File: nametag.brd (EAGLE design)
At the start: 33 x 20.3 mm, 23 parts, among them U1 MCP73831

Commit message: updated routes
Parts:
- D2: value (none) -> 3V
- LIPO: value LiPo Battery -> (none)
- moved IC1 22.2 mm to (14.0, 10.2), turned to 180 degrees
- moved PRO_MICRO 22.2 mm to (16.5, 10.2)
- moved TILT_SWITCH 21.9 mm to (26.0, 10.5), flipped to the bottom, turned to 180 degrees
- moved R9 21.9 mm to (12.1, 14.9), turned to 0 degrees
- moved C4 7.67 mm to (25.4, 6.35), flipped to the bottom, turned to 180 degrees
- moved C1 7.04 mm to (27.3, 7.30)
- moved D2 4.55 mm to (30.8, 1.91)
- moved R10 4.09 mm to (24.8, 8.89)
- moved R7 2.29 mm to (12.7, 5.08)
- moved R4 2.25 mm to (17.5, 14.9), turned to 0 degrees
- moved LIPO 2.03 mm to (5.08, 3.10), turned to 90 degrees
- moved R5 1.80 mm to (15.2, 5.71)
- moved R8 1.80 mm to (10.2, 5.08)
- moved R2 1.80 mm to (22.9, 14.6), turned to 0 degrees
- moved C2 1.55 mm to (24.4, 5.40)
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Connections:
- removed net D2: U1.1
- new net STAT: PRO_MICRO.10, U1.1
- new net VCC: PRO_MICRO.21, R9.2
- net +3V3: now also POWER.2; no longer POWER.1, PRO_MICRO.21, R9.2
- net GND: now also LIPO.2; no longer LIPO.1
- net LIPO: now also LIPO.1, POWER.1; no longer LIPO.2, POWER.2
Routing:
- net +3V3: track 0.00 -> 68.1 mm, vias 0 -> 3
- net WRITE: track 0.00 -> 33.0 mm, vias 0 -> 2
- net DATA: track 0.00 -> 31.8 mm, vias 0 -> 2
- net TILT: track 0.00 -> 29.1 mm, vias 0 -> 2
- net READ: track 0.00 -> 27.1 mm, vias 0 -> 2
- net COL2: track 0.00 -> 24.5 mm, vias 0 -> 1
- net COL3: track 0.00 -> 24.1 mm, vias 0 -> 1
- net STAT: track 0.00 -> 22.3 mm, vias 0 -> 3
- net CS: track 0.00 -> 21.4 mm, vias 0 -> 2
- net COL0: track 0.00 -> 15.0 mm, vias 0 -> 1
- net VIN: track 0.00 -> 14.5 mm
- net COL1: track 0.00 -> 14.0 mm, vias 0 -> 1
- net ROW7: track 0.00 -> 13.3 mm, vias 0 -> 1
- net ROW5: track 0.00 -> 12.9 mm, vias 0 -> 1
- net ROW6: track 0.00 -> 12.7 mm, vias 0 -> 1
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
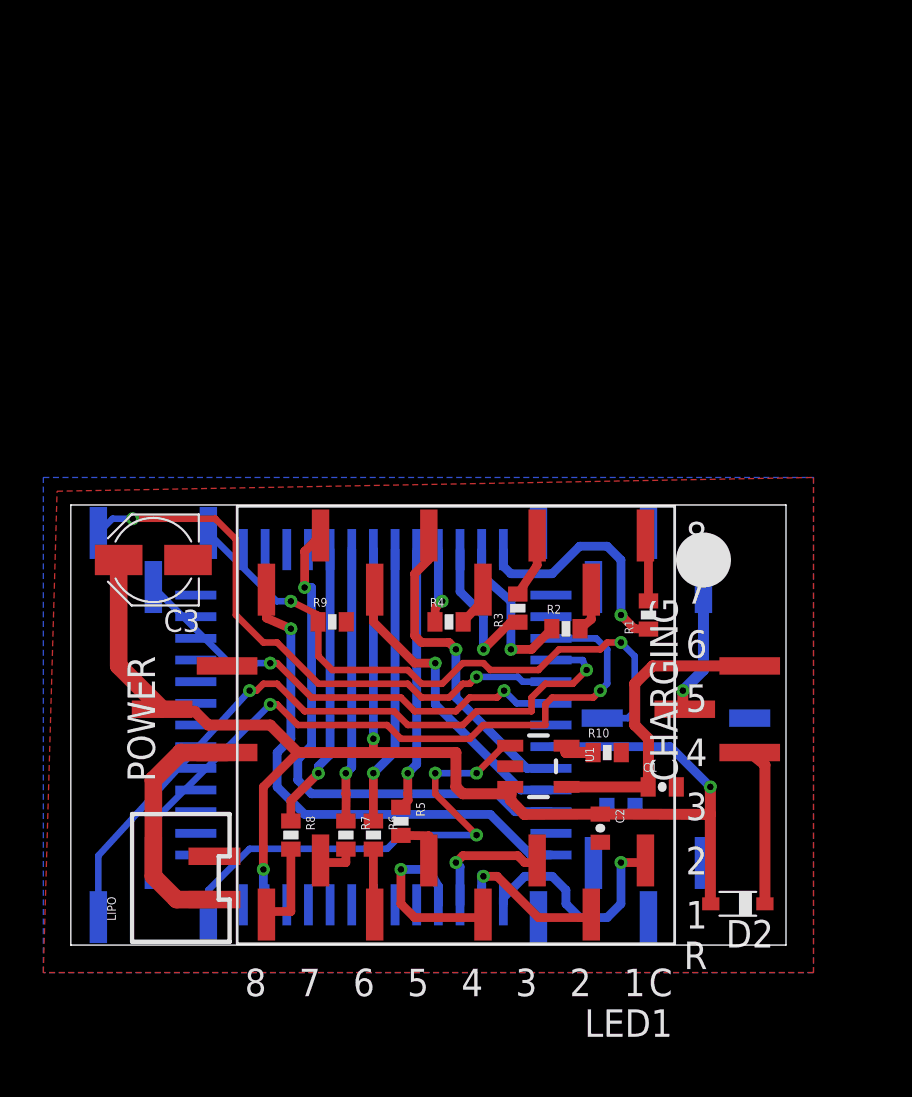
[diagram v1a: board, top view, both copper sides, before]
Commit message: added logos
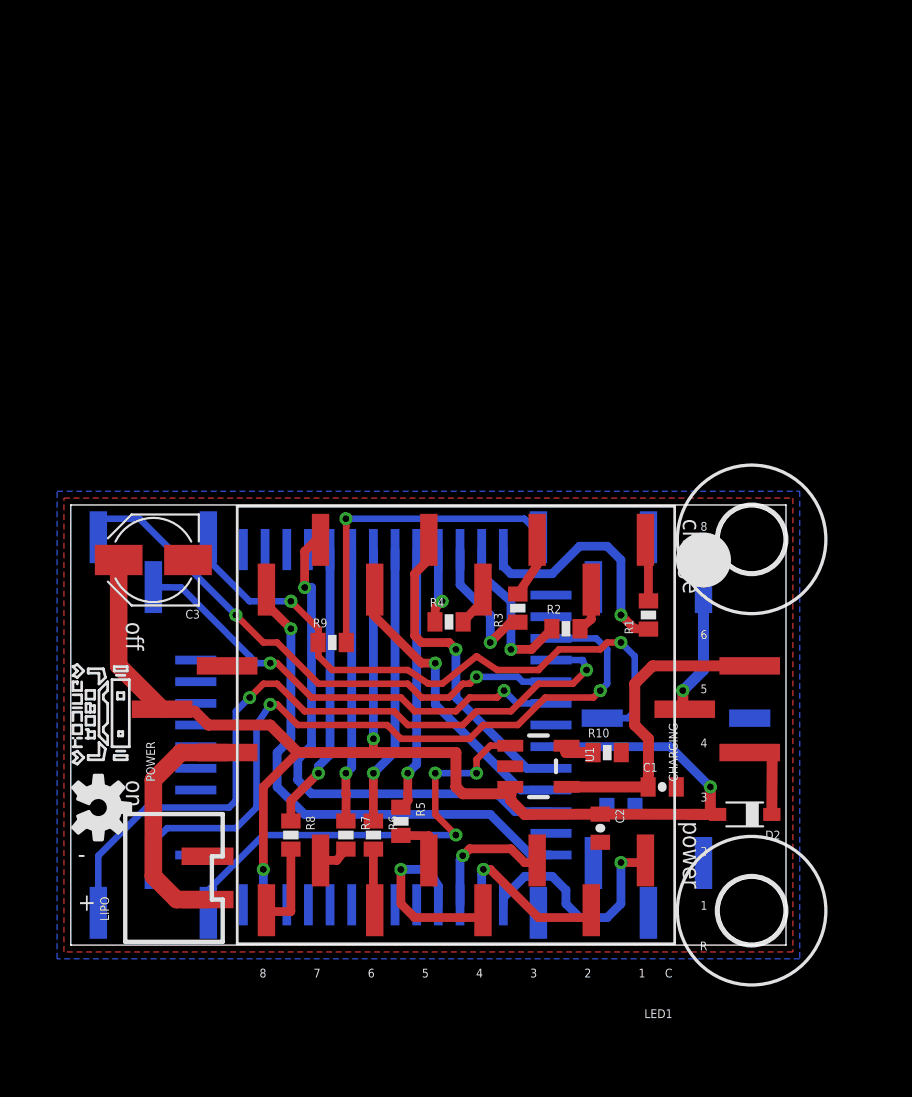
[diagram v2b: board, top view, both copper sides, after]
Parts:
- added E$1: (no value), Sumorobot:ROBOKODING-LOGO-S
- added LOGO1: OSHW-LOGOS, SparkFun-Aesthetics:OSHW-LOGO-S
- added U$1, U$2: (no value), holes:3,0
- moved D2 4.14 mm to (31.1, 6.03)
- moved R9 0.95 mm to (12.1, 14.0)
- moved LIPO 0.32 mm to (4.76, 3.10)
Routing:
- net VCC: track 0.00 -> 15.1 mm, vias 0 -> 1
- net +3V3: track 68.1 -> 64.6 mm
- net N$3: track 7.32 -> 3.98 mm
- net WRITE: track 33.0 -> 34.9 mm
- net READ: track 27.1 -> 25.6 mm
- net TILT: track 29.1 -> 30.5 mm
- net DATA: track 31.8 -> 33.0 mm
- net STAT: track 22.3 -> 21.3 mm
- net ROW2: track 7.17 -> 6.53 mm
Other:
- board text added: "+"
- board text added: "-"
- board text added: "NAMETAG v1.0"
- board text added: "charge"
- board text added: "off"
- board text added: "on"
- board text added: "power"

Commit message: updated nametag schematic and board
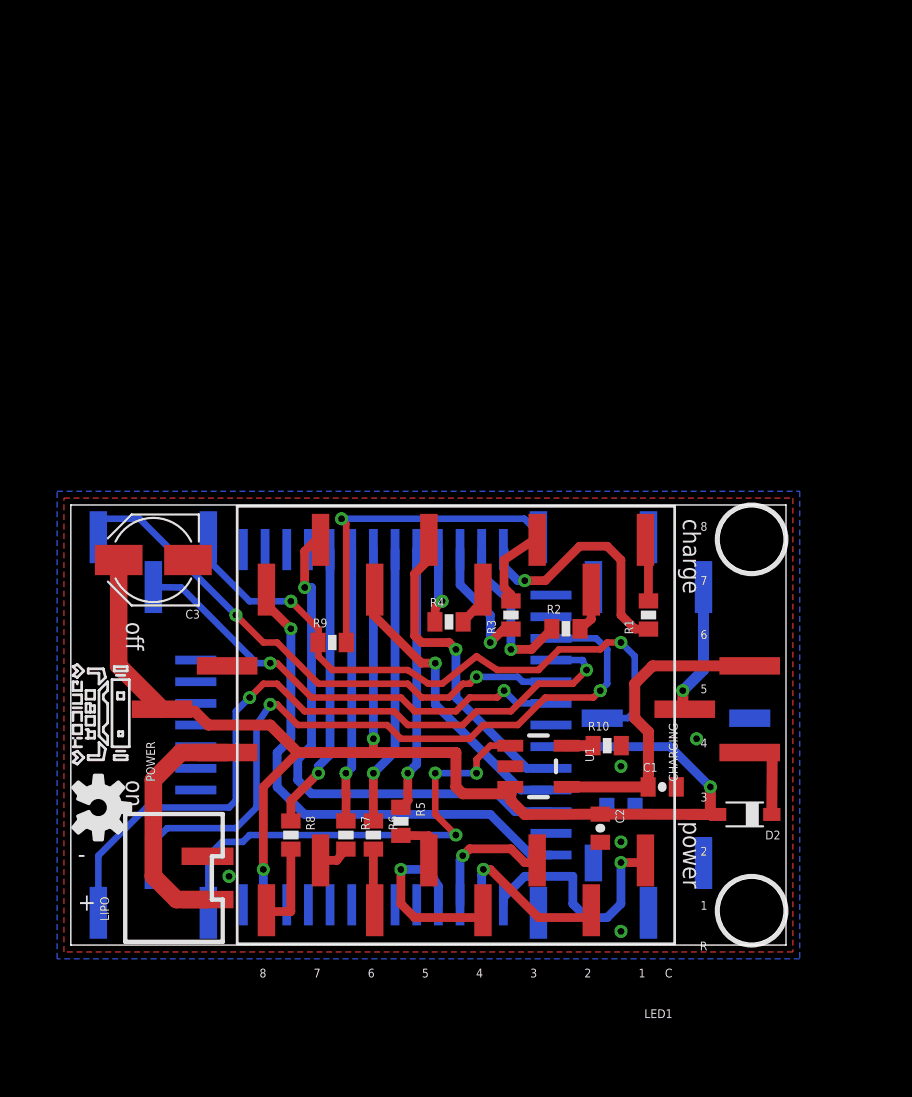
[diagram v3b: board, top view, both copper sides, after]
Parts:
- LOGO2: value (none) -> ROBOKODING-LOGOS
- moved R3 0.45 mm to (20.3, 15.2)
- moved R10 0.32 mm to (24.8, 9.21)
- renumbered E$1 to LOGO2
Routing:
- net N$4: track 2.97 -> 4.06 mm
- net STAT: track 21.3 -> 22.3 mm
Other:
- board text added: "Nametag"
- board text added: "v0.1"
- board text removed: "NAMETAG v1.0"
